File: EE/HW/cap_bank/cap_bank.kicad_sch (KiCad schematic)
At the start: 46 parts

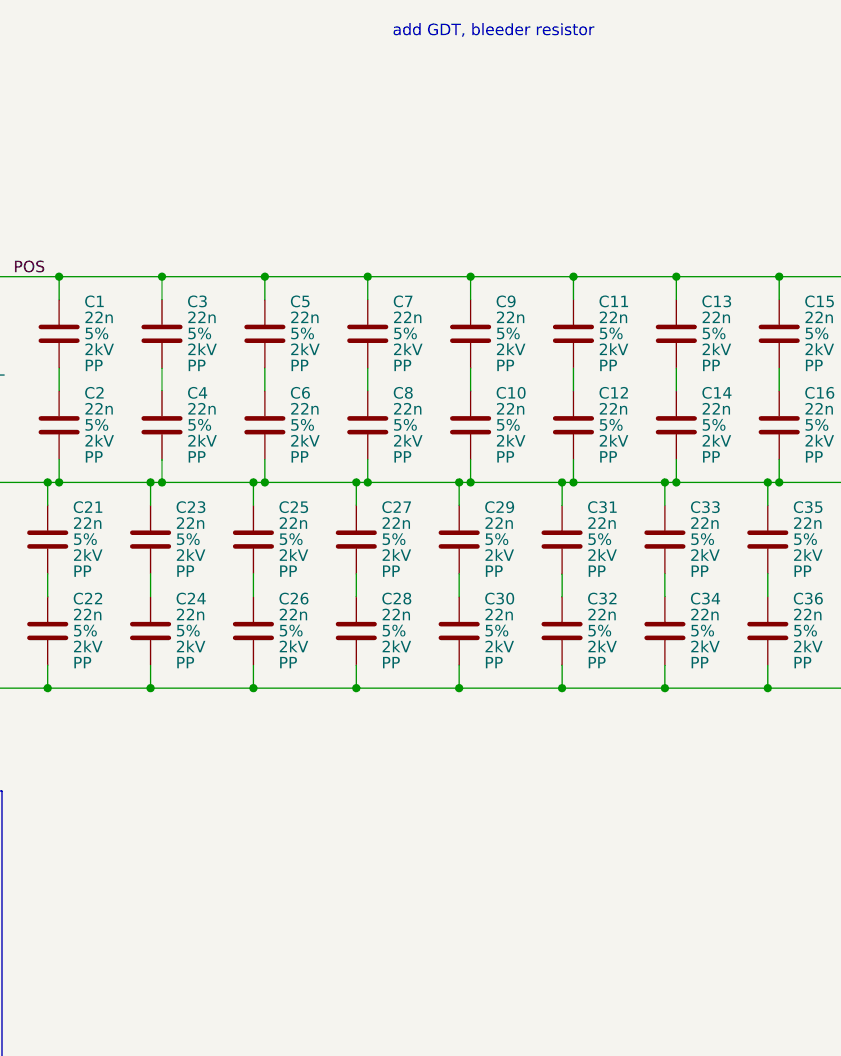
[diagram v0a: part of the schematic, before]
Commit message: progress on spice model and transformer design
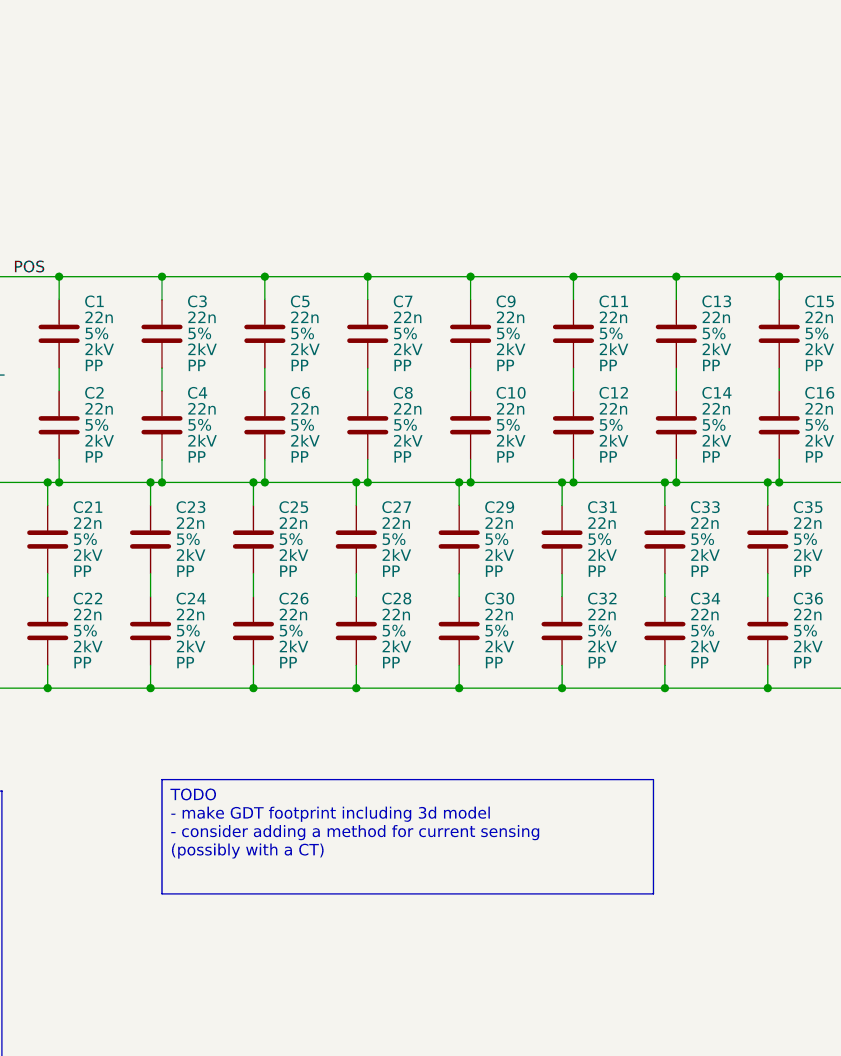
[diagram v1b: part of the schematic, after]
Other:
- note removed: "add GDT, bleeder resistor"
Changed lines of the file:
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@@
 	(generator_version "9.0")
 	(paper "A4")
-	(text "add GDT, bleeder resistor"
-		(exclude_from_sim no)
-		(at 148.59 50.292 0)
-		(effects
-			(font
-				(size 1.27 1.27)
-			)
-		)
-	)
 	(text_box "C_tot: 0.22uF, 4kV DC, 1400VRMS\nAt 50kHz, 64ARMS, 940VRMS\nbleed off tau: ~2.2s"
 		(exclude_from_sim no)
@@
 		(margins 0.9525 0.9525 0.9525 0.9525)
 		(stroke
+			(width 0)
+			(type solid)
+		)
+		(fill
+			(type none)
+		)
+		(effects
+			(font
+				(size 1.27 1.27)
+			)
+			(justify left top)
+		)
+	)
+	(text_box "TODO\n- make GDT footprint including 3d model\n- consider adding a method for current sensing (possibly with a CT)"
+		(exclude_from_sim no)
+		(at 111.76 133.35 0)
+		(size 54.61 12.7)
+		(margins 0.9525 0.9525 0.9525 0.9525)
+		(stroke

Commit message: order film cap bank pcba
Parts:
- removed GD1: CG32.5L, symbol peml:CG32.5L
- added C11, C12, C23, C24, C35, C36, C47, C48: 22n, peml:C_Rect_L26.5mm_W7.0mm_P22.50mm_R76, symbol peml_passives:R76UN22204040J
- added GD1: B88069X5690T502, peml:B88069X5690T502, symbol peml:B88069X5690T502
- added H3, H4, H5, H6: MountingHole, peml:MountingHole_4mm, symbol peml:MountingHole
- H1, H2: footprint MountingHole:MountingHole_8.4mm_M8_Pad_Via -> peml:Dual_M5_busbar_conn_24mm
- renumbered C19 to C10, C2 to C13, C4 to C14, C6 to C15, C8 to C16, C10 to C17, C12 to C18, C14 to C19, C3 to C2, C16 to C20, C18 to C21, C20 to C22, C21 to C25, C23 to C26, C25 to C27, C27 to C28, C5 to C3, C31 to C30, C33 to C31, C35 to C32, C37 to C33, C39 to C34, C22 to C37, C24 to C38, C26 to C39, C7 to C4, C28 to C40, C30 to C41, C32 to C42, C34 to C43, C36 to C44, C38 to C45, C40 to C46, C9 to C5, C11 to C6, C13 to C7, C15 to C8, C17 to C9, D2 to D1, D1 to D2
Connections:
- net NEG: now also C23.2, C24.2, C35.1, C36.1, GD1.1
- net POS: now also C11.1, C12.1, C47.2, C48.2, GD1.2
- new net: C36.2, C48.1
- new net: C12.2, C24.1
- new net: C35.2, C47.1
- new net: C11.2, C23.1
